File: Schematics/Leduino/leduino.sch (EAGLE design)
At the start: 36 parts, among them U1 MIC39100-5.0WS, U10 DMN6040SSD, U3 DMN6040SSD, U4 DMN6040SSD, U5 DMN6040SSD, U6 DMN6040SSD, U7 DMN6040SSD, U8 DMN6040SSD, U9 DMN6040SSD

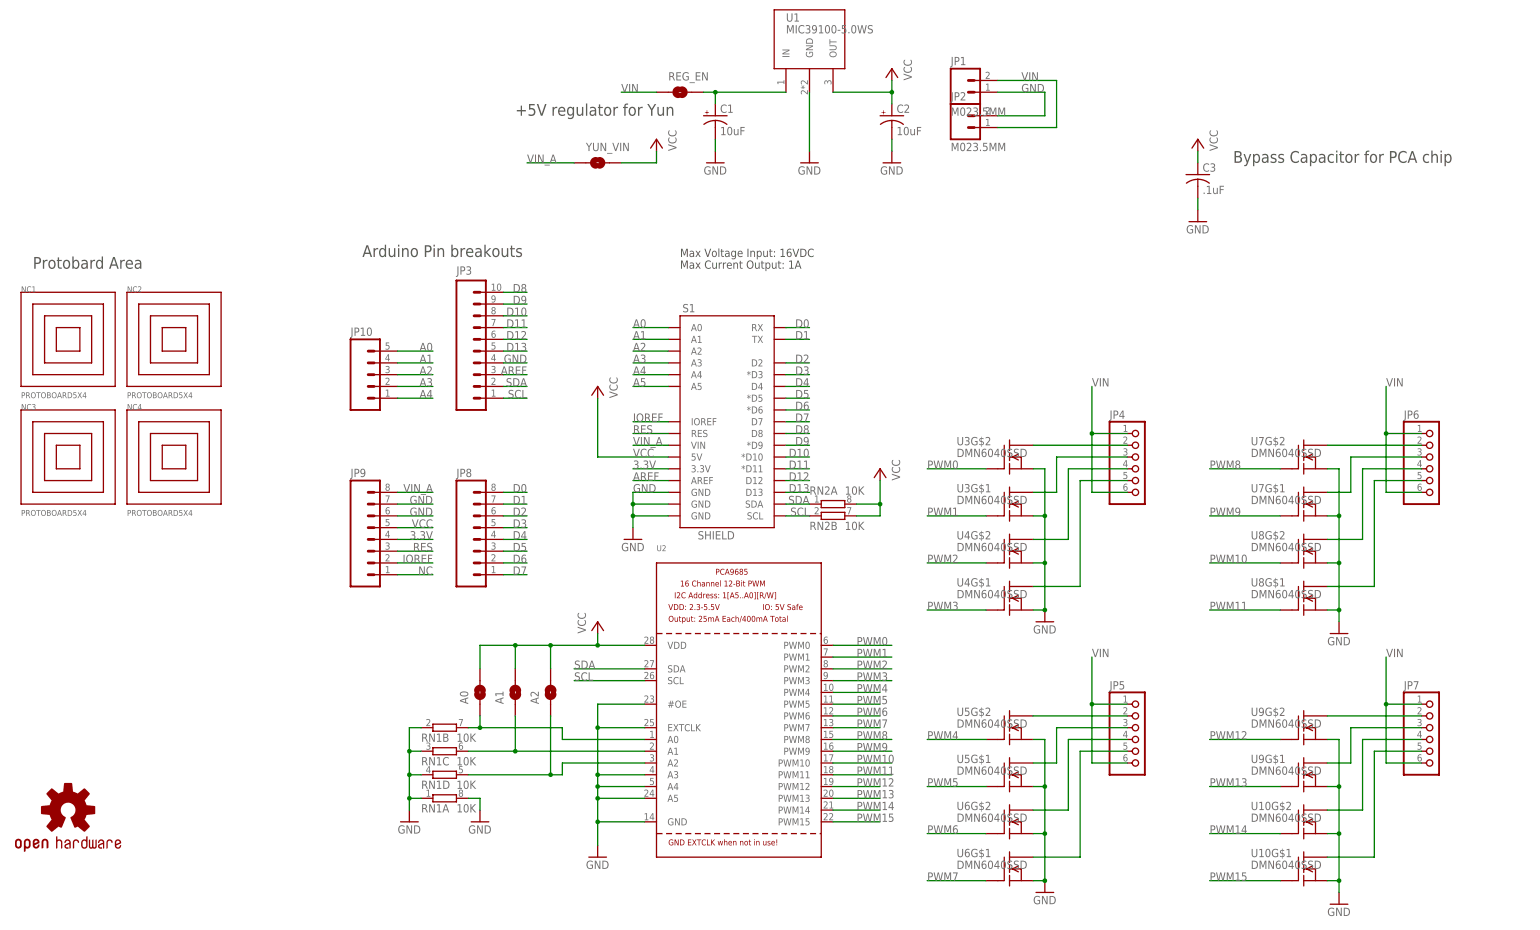
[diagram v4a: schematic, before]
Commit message: Finished v2 update, ready for lbr cleanup
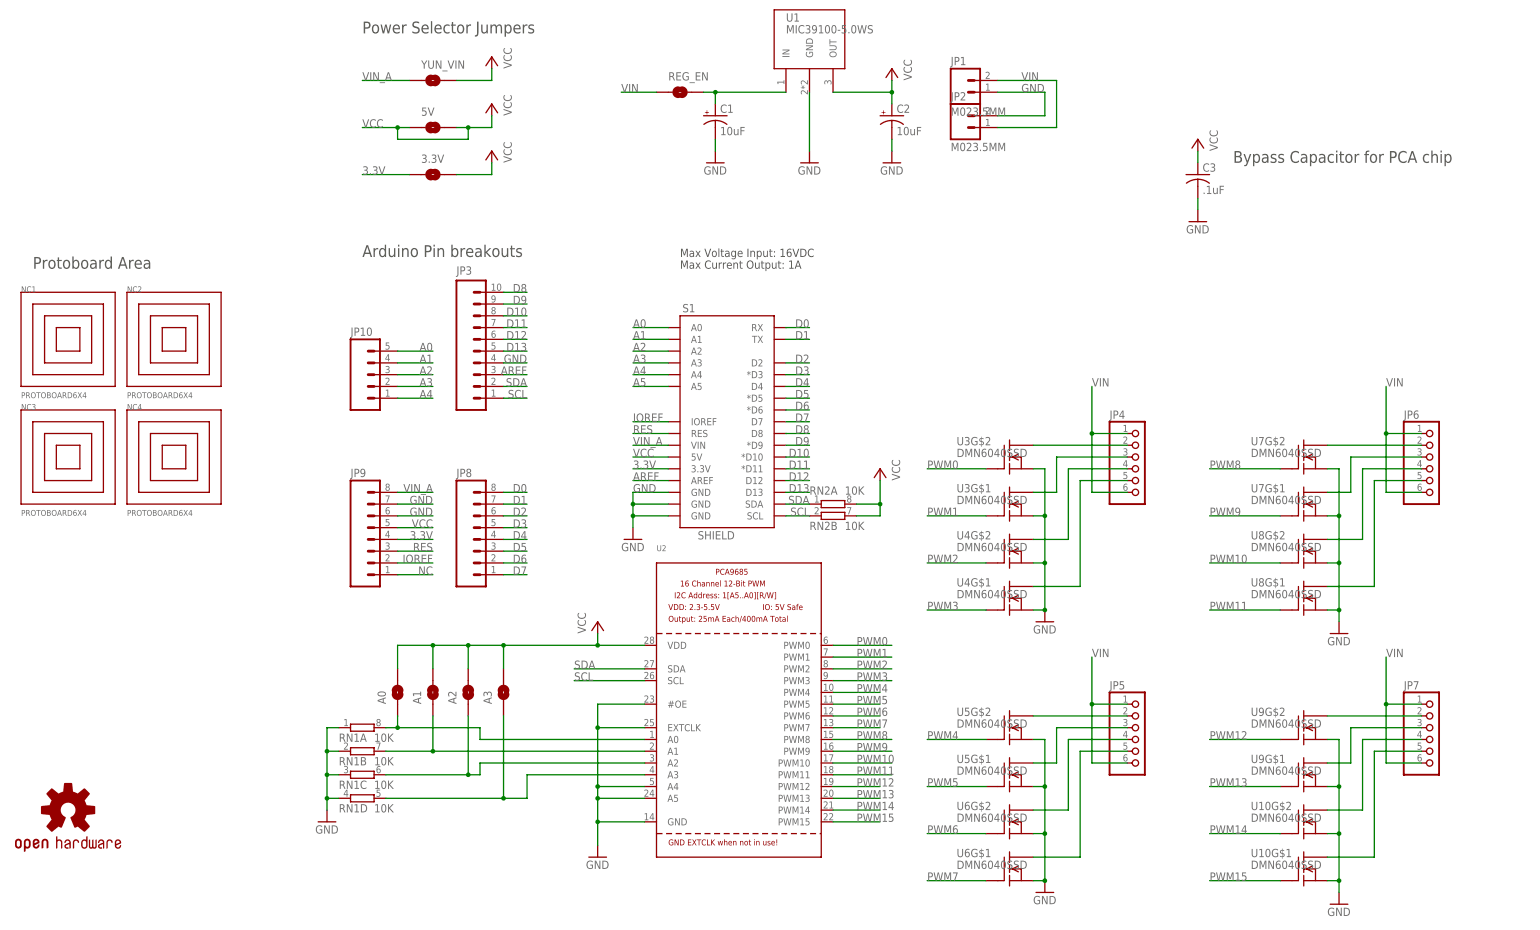
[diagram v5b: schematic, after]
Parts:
- removed U$1: OSHW-LOGOL, Pro_Micro:OSHW-LOGOL
- added 3.3V, 5V, A3: SOLDERJUMPERNO, Leduino:SOLDERJUMPERNO
- added U$6: OSHW-LOGOM, Pro_Micro:OSHW-LOGOM
- NC1, NC2, NC3, NC4: value PROTOBOARD5X4 -> PROTOBOARD6X4; device Leduino:PROTOBOARD5X4 -> Leduino:PROTOBOARD6X4
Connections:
- new net N$14: A3.1, RN1D.2, U2.A3
- net 3.3V: now also 3.3V.1
- net GND: no longer RN1A.2, U2.A3
- net N$15: now also RN1A.2; no longer RN1B.2
- net N$16: now also RN1B.2; no longer RN1C.2
- net N$21: now also RN1C.2; no longer RN1D.2
- net VCC: now also 3.3V.2, 5V.1, 5V.2, A3.2
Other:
- note added: "Power Selector Jumpers"
- note added: "Protoboard Area"
- note removed: "+5V regulator for Yun"
- note removed: "Protobard Area"
- moved on the sheet: A0, A1, A2, RN1A, RN1B, RN1C, RN1D, YUN_VIN
